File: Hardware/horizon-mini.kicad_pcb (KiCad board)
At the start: 2 copper layers, 34 x 41.8 mm, 92 parts, among them J19 Screw_Terminal_01x02, J2 Screw_Terminal_01x02, J20 Screw_Terminal_01x02, J3 Micro_SD_Card_Det1, J7 USB_C_Receptacle_USB2.0_16P, J8 Conn_02x03_Counter_Clockwise, Q1 BSS138, Q10 DMG2301L, Q8 IRLML6402, Q9 IRLML6402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

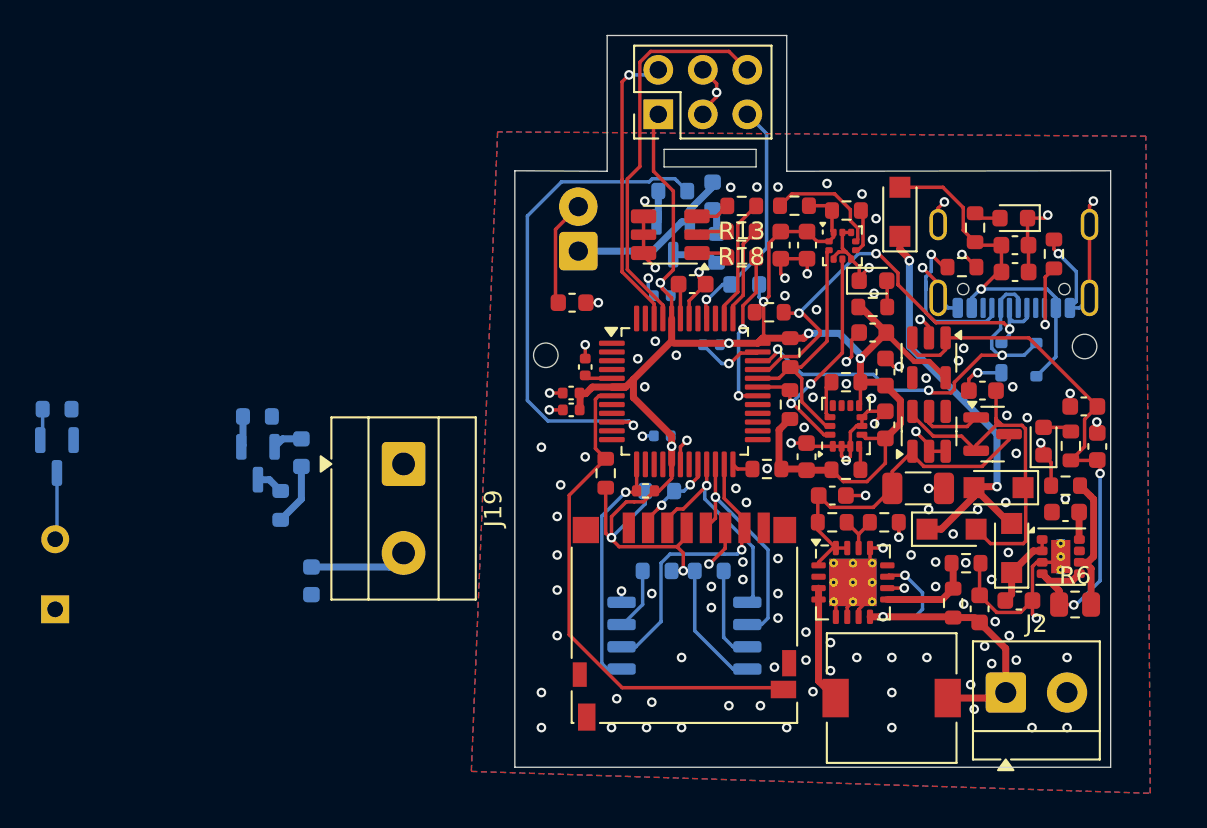
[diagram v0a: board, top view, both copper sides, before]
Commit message: uuuh, starting buzzer wiring while I'm waiting for max's amazing footprint ;)
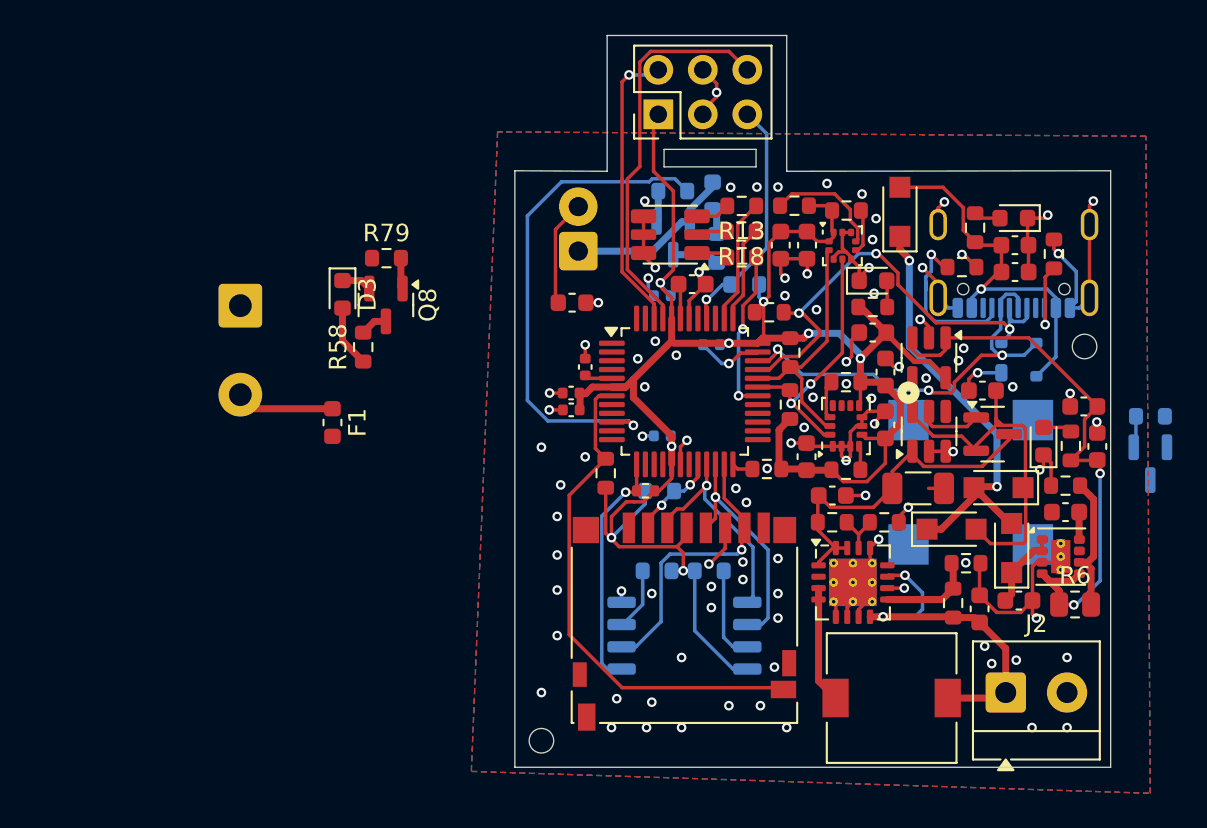
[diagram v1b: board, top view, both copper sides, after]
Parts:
- BZ2: footprint Buzzer_Beeper:MagneticBuzzer_PUI_AT-0927-TT-6-R -> SMD_BUZZ:MLT-8530_JHE
- D3, F1, Q8, R58, R79: moved to F.Cu
- J19: moved to B.Cu
- moved R1 62.4 mm to (172.3, 116.5)
- moved Q1 62.4 mm to (172.2, 119.2)
- moved BZ2 52.8 mm to (162.0, 120.2), turned to -90 degrees
- moved REF** 22.0 mm to (137.5, 135.0)
- moved J19 13.0 mm to (120.3, 110.2)
- moved R79 11.7 mm to (128.7, 107.5), turned to 0 degrees
- moved Q8 11.6 mm to (128.6, 110.1)
- moved R58 10.2 mm to (127.3, 112.5)
- moved D3 9.33 mm to (126.1, 109.5)
- moved F1 9.11 mm to (125.6, 116.8)
- moved G*** 6.10 mm to (146.9, 119.2)
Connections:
- BZ2 pad 1: +3.3V -> (no net)
- BZ2 pad 2: Net-(BZ2--) -> (no net)
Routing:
- net Net-(BZ2--): track 3.82 -> 0.00 mm
- net (no net): track 2.01 -> 0.00 mm
- net GND: track 94.5 -> 95.9 mm, vias 124 -> 94

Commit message: please look it over, I'm finished with it
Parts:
- removed D3, D4: LED, LED_SMD:LED_0603_1608Metric
- removed F1: Polyfuse, Fuse:Fuse_0603_1608Metric
- removed J19: Screw_Terminal_01x02, TerminalBlock_MetzConnect:TerminalBlock_MetzConnect_Type101_RT01602HBWC_1x02_P5.08mm_Horizontal
- removed J20: Screw_Terminal_01x02, TerminalBlock_Phoenix:TerminalBlock_Phoenix_MPT-0,5-2-2.54_1x02_P2.54mm_Horizontal
- removed Q8, Q9: IRLML6402, Package_TO_SOT_SMD:SOT-23
- removed R58, R59: 1k, Resistor_SMD:R_0603_1608Metric
- removed R79, R81: 100, Resistor_SMD:R_0603_1608Metric
- added ?: , , F.Cu at (137.0, 120.2)
- added D2: LED, LED_SMD:LED_0603_1608Metric, B.Cu at (137.5, 109.8)
- added J1: Screw_Terminal_01x02, TerminalBlock_Phoenix:TerminalBlock_Phoenix_MPT-0,5-2-2.54_1x02_P2.54mm_Horizontal, B.Cu at (139.6, 104.5)
- added J16: arming terminal, Connector_PinHeader_2.00mm:PinHeader_1x02_P2.00mm_Vertical_SMD_Pin1Left, B.Cu at (146.1, 105.0)
- added Q2: IRLML6402, Package_TO_SOT_SMD:SOT-23, B.Cu at (138.0, 113.8)
- added R30: 100, Resistor_SMD:R_0603_1608Metric, B.Cu at (136.8, 117.0)
- added R31: 1k, Resistor_SMD:R_0603_1608Metric, B.Cu at (137.5, 111.3)
- added R80: 10k, Resistor_SMD:R_0603_1608Metric, B.Cu at (139.8, 110.5)
- F2: moved to B.Cu
- moved G*** 24.9 mm to (165.8, 135.5)
- moved R1 21.4 mm to (156.1, 130.5), turned to 90 degrees
- moved Q1 17.6 mm to (158.8, 130.5), turned to 0 degrees
- moved F2 2.12 mm to (141.3, 110.6), turned to -90 degrees
- turned BZ2 to 90 degrees
- turned C6 to 0 degrees
- turned C7 to 180 degrees
- turned C8 to 180 degrees
- turned C9 to 180 degrees
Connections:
- BZ2 pad 1: (no net) -> Net-(BZ2)
- BZ2 pad 2: (no net) -> +3.3V
- D14 pad 2: Net-(D14-I/O1) -> D+ DMCU-2
- D14 pad 3: Net-(D14-I/O2) -> D- DMCU-2
- J7 pad A6: Net-(D14-I/O1) -> D+ DMCU-2
- J7 pad A7: Net-(D14-I/O2) -> D- DMCU-2
- J7 pad B6: Net-(D14-I/O1) -> D+ DMCU-2
- J7 pad B7: Net-(D14-I/O2) -> D- DMCU-2
- Q1 pad 3: Net-(BZ2--) -> Net-(BZ2)
- U5 pad 17: GND -> +3.3V
- U5 pad 36: GND -> +3.3V
- U5 pad 44: GND -> +3.3V
- U5 pad 6: GND -> +3.3V
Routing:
- net BUZZER: track 1.82 -> 41.6 mm, vias 0 -> 1
- net mosfet2_signalfire: track 28.8 -> 0.00 mm, vias 1 -> 0
- net +5V: track 24.9 -> 41.3 mm
- net +3.3V: track 116.5 -> 129.2 mm, vias 10 -> 9
- net GND: track 95.9 -> 106.1 mm, vias 94 -> 136
- net Net-(D4-K): track 9.86 -> 0.00 mm
- net Net-(D2-K): track 0.00 -> 9.48 mm
- net Net-(BZ2): track 0.00 -> 9.11 mm
- net Net-(J16-Pin_2): track 0.00 -> 8.42 mm
- net POWAAAA: track 21.0 -> 27.4 mm
- net mosfet1_signalfire: track 0.00 -> 6.00 mm, vias 0 -> 1
- net nRESET DMCU-2: track 14.0 -> 19.7 mm
- net Net-(J19-Pin_2): track 5.59 -> 0.00 mm
- net Net-(Q2-D): track 0.00 -> 4.20 mm
- net Net-(L7-Pad2): track 6.68 -> 10.3 mm
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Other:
- outline, holes or cut-outs redrawn
- board text added: "V1.0"
- board text removed: "Hardware by: Scooter Meddy B"
- board text removed: "V1.0 © 2025 Horizon Avionics"

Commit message: forgot to push from last night. Very small silscreen changes and stuff
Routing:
- net GND: track 106.1 -> 107.8 mm
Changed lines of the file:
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@@
 	)
 	(segment
+		(start 140.0875 133.65)
+		(end 140.9 133.65)
+		(width 0.4)
+		(layer "F.Cu")
+		(net 2)
+	)
+	(segment
 		(start 157.922345 113.64601)
 		(end 157.600931 113.64601)
@@
 	)
 	(segment
+		(start 140.9 133.65)
+		(end 141.5 134.25)
+		(width 0.4)
+		(layer "F.Cu")
+		(net 2)
+	)
+	(segment
 		(start 156.253661 124.740007)
 		(end 156.378661 124.865007)
@@
 	)
 	(segment
-		(start 148.851 100.649)
-		(end 149.25 100.25)
+		(start 143.501292 100.898766)
+		(end 143.751058 100.649)
 		(width 0.2)
 		(layer "B.Cu")
@@
 	)
 	(segment
-		(start 148.275746 107.375688)
-		(end 143.399 102.498942)
+		(start 149.25 100.25)
+		(end 149.25 99.25)
 		(width 0.2)
 		(layer "B.Cu")
@@
 	)
 	(segment
-		(start 149.25 100.25)
-		(end 149.25 99.25)
+		(start 148.851 100.649)
+		(end 149.25 100.25)
 		(width 0.2)
 		(layer "B.Cu")
@@
 	)
 	(segment
-		(start 143.399 102.498942)
-		(end 143.399 101.001058)
+		(start 148.275746 107.375688)
+		(end 143.501292 102.601234)
 		(width 0.2)
 		(layer "B.Cu")
@@
 	)
 	(segment
-		(start 147.504561 109.732048)
-		(end 148.275746 108.960863)
+		(start 148.275746 108.960863)
+		(end 148.275746 107.375688)
 		(width 0.2)
 		(layer "B.Cu")
@@
 	)
 	(segment
-		(start 143.399 101.001058)
-		(end 143.751058 100.649)
+		(start 143.751058 100.649)
+		(end 148.851 100.649)
 		(width 0.2)
 		(layer "B.Cu")
@@
 	)
 	(segment
-		(start 148.275746 108.960863)
-		(end 148.275746 107.375688)
+		(start 147.504561 109.732048)
+		(end 148.275746 108.960863)
 		(width 0.2)
 		(layer "B.Cu")
@@
 	)
 	(segment
-		(start 143.751058 100.649)
-		(end 148.851 100.649)
+		(start 143.501292 102.601234)
+		(end 143.501292 100.898766)
 		(width 0.2)
 		(layer "B.Cu")
@@
 	)
 	(segment
-		(start 137.899 131.899)
-		(end 137.899 121.101)
+		(start 140.25 118.75)
+		(end 140.25 117.75)
 		(width 0.2)
 		(layer "B.Cu")
@@
 	)
 	(segment
-		(start 140.25 118.75)
-		(end 140.25 117.75)
+		(start 156.070027 131.303671)
+		(end 151.873698 135.5)
 		(width 0.2)
 		(layer "B.Cu")
@@
 	)
 	(segment
-		(start 137.899 121.101)
-		(end 140.25 118.75)
+		(start 137.899 131.899)
+		(end 137.899 121.101)
 		(width 0.2)
 		(layer "B.Cu")
@@
 	)
 	(segment
-		(start 151.873698 135.5)
-		(end 141.5 135.5)
+		(start 137.899 121.101)
+		(end 140.25 118.75)
 		(width 0.2)
 		(layer "B.Cu")
@@
 	)
 	(segment
-		(start 156.070027 131.303671)
-		(end 151.873698 135.5)
+		(start 151.873698 135.5)
+		(end 141.5 135.5)
 		(width 0.2)
 		(layer "B.Cu")
@@
 		(polygon
 			(pts
-				(xy 164.98089 134.149071) (xy 169.180475 134.149071) (xy 169.221953 136.010369) (xy 164.322437 136.020738)
-				(xy 164.363914 134.154256) (xy 164.99126 134.154256)
+				(xy 164.98089 134.149071) (xy 169.25 134.149071) (xy 169.25 136.25) (xy 164.322437 136.25) (xy 164.363914 134.154256)
+				(xy 164.99126 134.154256)
 			)
 		)

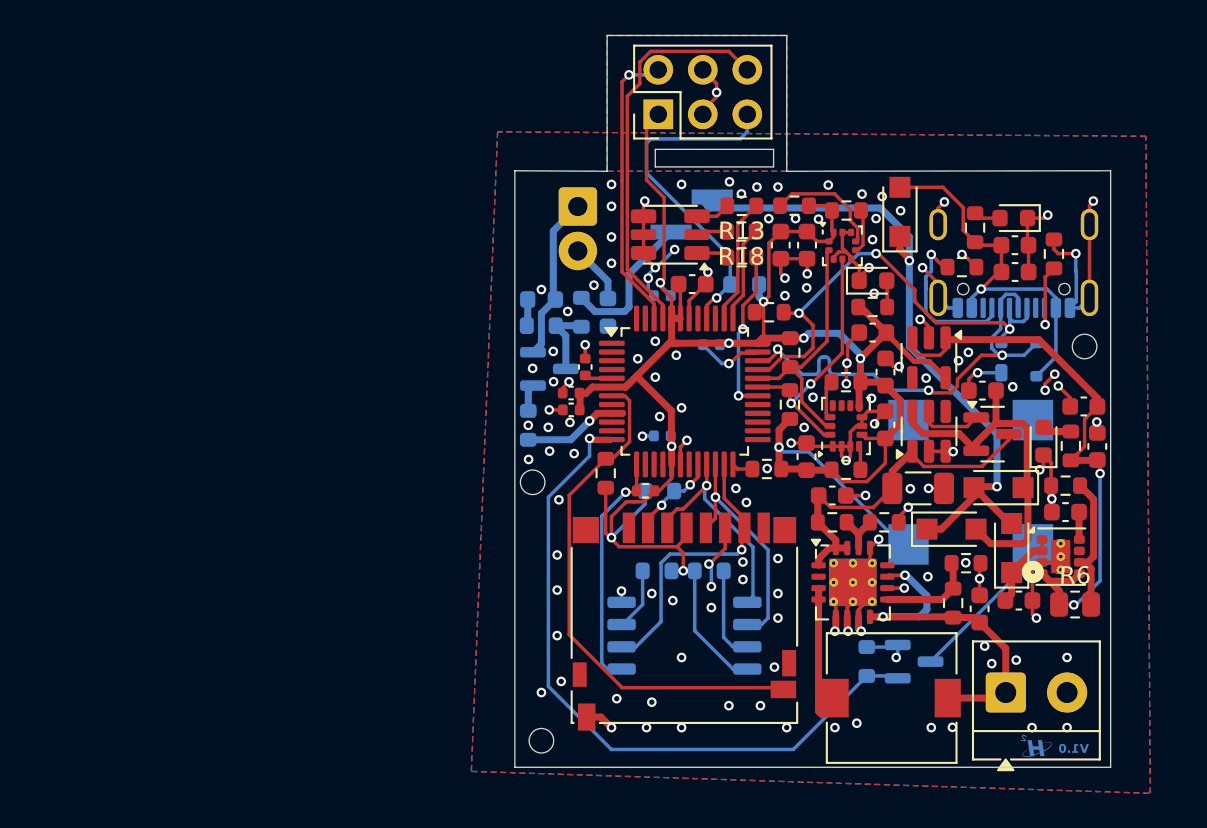
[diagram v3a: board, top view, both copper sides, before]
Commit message: @mpkendall review before ordering pplllease. I fixed the data lines.
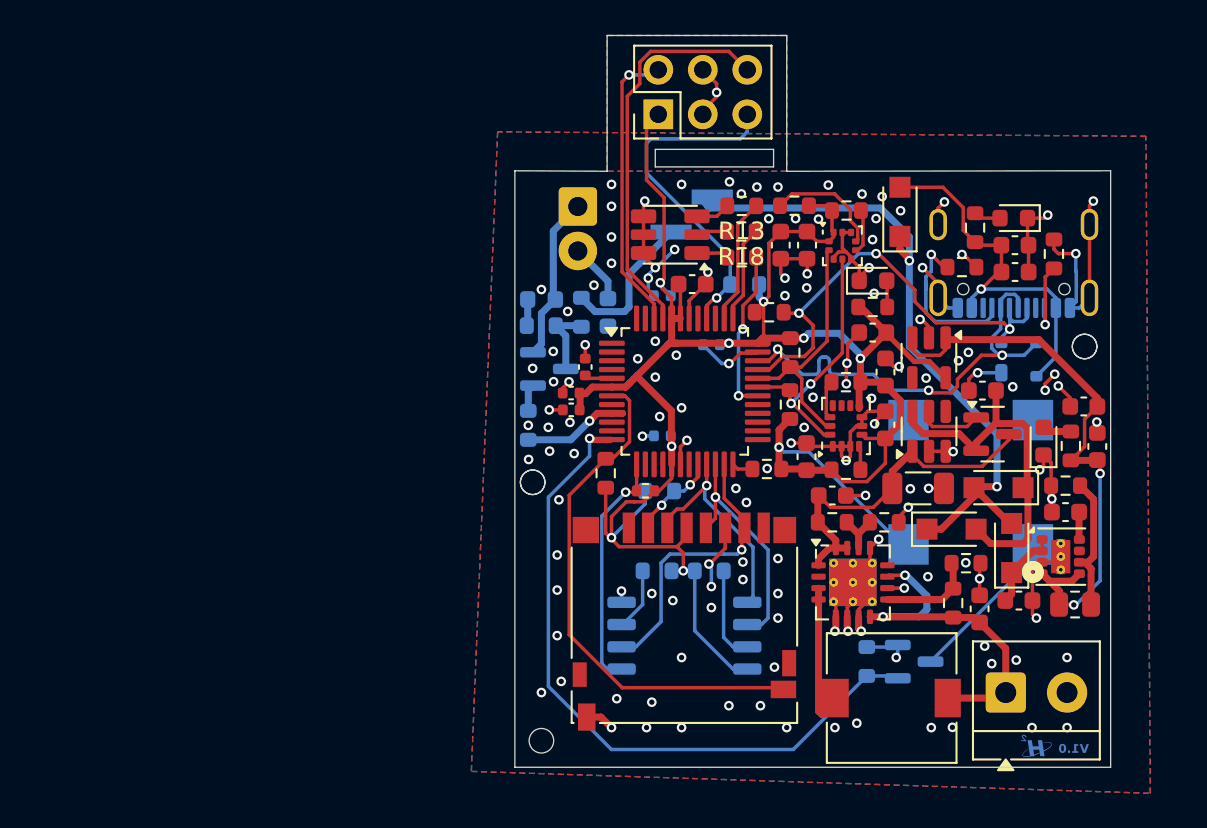
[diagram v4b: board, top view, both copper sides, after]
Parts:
- removed the ? at (137.0, 120.2)
- removed the REF** at (137.5, 135.0)
- added ?: , , F.Cu at (168.5, 112.5)
- added ? (x2): , , F.Cu at (137.0, 120.2)
- added ?: , , F.Cu at (137.5, 135.0)
- J2: value Screw_Terminal_01x02 -> Conn_01x02_Pin
- turned C11 to 0 degrees
- turned C12 to 180 degrees
- turned C7 to 0 degrees
- turned C8 to 0 degrees
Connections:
- net D+ DMCU-2 renamed Net-(D14-I/O1)
- net D- DMCU-2 renamed Net-(D14-I/O2)
- C11 pad 1: +3.3V -> GND
- C11 pad 2: GND -> +3.3V
- C12 pad 1: GND -> +3.3V
- C12 pad 2: +3.3V -> GND
- C7 pad 1: +3.3V -> GND
- C7 pad 2: GND -> +3.3V
- C8 pad 1: +3.3V -> GND
- C8 pad 2: GND -> +3.3V
- U5 pad 10: mosfet2_signalfire -> unconnected-(U5-PA05-Pad10)

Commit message: @mpkendall please review before ordering.
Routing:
- net GND: track 107.8 -> 110.8 mm
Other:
- outline, holes or cut-outs redrawn
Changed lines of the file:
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@@
 	)
 	(gr_rect
-		(start 144 101.25)
+		(start 143.724967 101.25)
 		(end 150.75 102.25)
 		(stroke
@@
 	)
 	(segment
+		(start 143.021263 100.398737)
+		(end 144.17 99.25)
+		(width 0.2)
+		(layer "F.Cu")
+		(net 1)
+	)
+	(segment
 		(start 145.4325 109.044259)
 		(end 145.328526 108.940285)
@@
 	)
 	(segment
-		(start 144.501 104)
-		(end 143.5 102.999)
-		(width 0.2)
-		(layer "F.Cu")
-		(net 1)
-	)
-	(segment
 		(start 145.7875 123.377)
 		(end 145.2385 123.926)
@@
 	)
 	(segment
-		(start 144.287495 108.863018)
-		(end 144.501 108.649513)
-		(width 0.2)
-		(layer "F.Cu")
-		(net 1)
-	)
-	(segment
 		(start 139.708542 115.190285)
 		(end 139.67448 115.156223)
@@
 	)
 	(segment
-		(start 143.5 99.92)
-		(end 144.17 99.25)
-		(width 0.2)
-		(layer "F.Cu")
-		(net 1)
-	)
-	(segment
 		(start 153.914161 106.502854)
 		(end 153.220573 106.502854)
@@
 	)
 	(segment
+		(start 144.501 108.649513)
+		(end 144.501 104)
+		(width 0.2)
+		(layer "F.Cu")
+		(net 1)
+	)
+	(segment
+		(start 144.287495 108.863018)
+		(end 144.501 108.649513)
+		(width 0.2)
+		(layer "F.Cu")
+		(net 1)
+	)
+	(segment
 		(start 144.9325 117.597446)
 		(end 144.917527 117.582473)
@@
 	)
 	(segment
+		(start 144.501 104)
+		(end 143.021263 102.520263)
+		(width 0.2)
+		(layer "F.Cu")
+		(net 1)
+	)
+	(segment
 		(start 144.224737 120.739203)
 		(end 144.9325 120.03144)
@@
 	)
 	(segment
+		(start 143.021263 102.520263)
+		(end 143.021263 100.398737)
+		(width 0.2)
+		(layer "F.Cu")
+		(net 1)
+	)
+	(segment
 		(start 157.1307 119.159349)
 		(end 157.1307 117.747383)
@@
 	)
 	(segment
-		(start 143.5 102.999)
-		(end 143.5 99.92)
-		(width 0.2)
-		(layer "F.Cu")
-		(net 1)
-	)
-	(segment
 		(start 149.845 112.314848)
 		(end 150.135518 112.02433)
@@
 	)
 	(segment
-		(start 144.501 108.649513)
-		(end 144.501 104)
-		(width 0.2)
-		(layer "F.Cu")
-		(net 1)
-	)
-	(segment
 		(start 144.9325 111.25)
 		(end 144.9325 110.902348)
@@
 	)
 	(segment
+		(start 167.140253 123.742122)
+		(end 167.140253 125.242122)
+		(width 0.2)
+		(layer "F.Cu")
+		(net 2)
+	)
+	(segment
 		(start 167 107.2)
 		(end 166.75 106.95)
@@
 	)
 	(segment
+		(start 167.140253 124.492122)
+		(end 167.140253 125.242122)
+		(width 0.2)
+		(layer "B.Cu")
+		(net 2)
+	)
+	(segment
 		(start 146.72 112.4)
 		(end 147.792635 113.472635)
@@
 	)
 	(segment
+		(start 167.140253 123.742122)
+		(end 167.140253 124.492122)
+		(width 0.2)
+		(layer "B.Cu")
+		(net 2)
+	)
+	(segment
 		(start 168.027249 108.227249)
 		(end 168.027249 109.933323)
@@
 	)
 	(segment
-		(start 143.501292 100.898766)
-		(end 143.751058 100.649)
+		(start 148.275746 107.375688)
+		(end 143.307957 102.407899)
 		(width 0.2)
 		(layer "B.Cu")
@@
 	)
 	(segment
-		(start 149.25 100.25)
-		(end 149.25 99.25)
+		(start 148.275746 108.960863)
+		(end 148.275746 107.375688)
 		(width 0.2)
 		(layer "B.Cu")
@@
 	)
 	(segment
-		(start 148.851 100.649)
-		(end 149.25 100.25)
+		(start 143.307957 102.407899)
+		(end 143.307957 101.092101)
 		(width 0.2)
 		(layer "B.Cu")
@@
 	)
 	(segment
-		(start 148.275746 107.375688)
-		(end 143.501292 102.601234)
+		(start 148.851 100.649)
+		(end 149.25 100.25)
 		(width 0.2)
 		(layer "B.Cu")
@@
 	)
 	(segment
-		(start 148.275746 108.960863)
-		(end 148.275746 107.375688)
+		(start 143.307957 101.092101)
+		(end 143.751058 100.649)
 		(width 0.2)
 		(layer "B.Cu")
@@
 	)
 	(segment
-		(start 147.504561 109.732048)
-		(end 148.275746 108.960863)
+		(start 149.25 100.25)
+		(end 149.25 99.25)
 		(width 0.2)
 		(layer "B.Cu")
@@
 	)
 	(segment
-		(start 143.501292 102.601234)
-		(end 143.501292 100.898766)
+		(start 147.504561 109.732048)
+		(end 148.275746 108.960863)
 		(width 0.2)
 		(layer "B.Cu")
